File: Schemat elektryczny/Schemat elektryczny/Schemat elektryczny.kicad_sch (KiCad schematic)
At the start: 15 parts, among them M1 Pompa Membranowa R385: 1, M2 Pompa Membranowa R385: 2, M3 Motor_Servo MG-90S, Q2 BC107, Q3 BC107, U1 ESP32-WROOM-32, U10 HX711: 1, U2 Socket 230V AC, U3 Converter 230/12V AC/DC, U4 Converter 12/5V DC/DC, U5 Strain gauge: 3, U6 HX711: 3, U7 Strain gauge: 2, U8 HX711: 2, U9 Strain gauge: 1

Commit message: Squashed commit of the following:
commit 14932f831172e4170d33ec92addd128a30fe4f06
Author: Brajan Gąbka <104710627+Duke-Axer@users.noreply.github.com>
Date:   Sun Mar 23 11:26:04 2025 +0100

    Dodałem bibliotekę od serwomechanizmu i rozwinąłem funkcje od servo. Zmodyfikowałem schemat elektryczny. (#5)

    Co-authored-by: Brajan <b.gabka.nkn@gmail.com>
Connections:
- net at U6. (UCC): now also U1.25 (GPIO25); no longer U5. (A+)
- net at U10. (UCC): now also U1.27 (GPIO27); no longer U9. (A+)
- net at U2. (Neutral): now also U3. (-12V)
- net at U3. (-12V): now also M1.2 (-), M2.2 (-), U4. (-5V); no longer U2. (Neutral)
- net at U8. (UCC): now also U1.26 (GPIO26); no longer U7. (A+)
- new net: U5. (A+), U6. (UCC) (x3)
- new net: U10. (UCC), U9. (A+) (x3)
- new net: U2. (Neutral), U3. (-12V)
- new net: M3.2 (+), U1. (-5V), U4. (-5V)
- new net: M3.3 (-), U1. (-5V), U4. (-5V)
- new net: U10. (UCC), U6. (UCC), U8. (UCC)
- new net: U1. (-5V), U10. (UCC), U6. (UCC), U8. (UCC)
- new net: U1. (-5V), U1.22 (CLK), U10. (UCC), U6. (UCC), U8. (UCC)
- new net: U7. (A+), U8. (UCC) (x3)
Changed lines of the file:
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@@
 		(date "2025-03-21")
 		(company "Politechnika Lubelska")
-		(comment 1 "Patrycja Demianiuk")
-		(comment 2 "Daniel Cichocki")
-		(comment 3 "Brajan Gąbka")
+		(comment 1 "Inż Patrycja Demianiuk")
+		(comment 2 "Inż Daniel Cichocki")
+		(comment 3 "Inż Brajan Gąbka")
 		(comment 4 "Internet Rzeczy")
 		(comment 5 "Pani mgr inż. Aleksandra Wilczyńska")

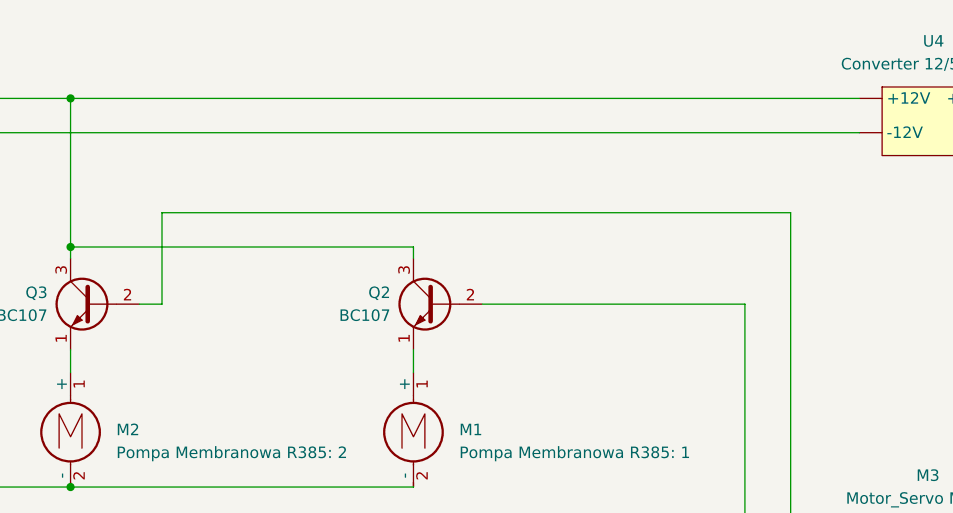
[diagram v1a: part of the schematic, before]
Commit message: Gabka (#11)
* dodałem plik .gitignore i usunąłem śledzenie folderu z schematów elektrycznych backups

* Dodałem rezystory do schematu

* Poprawiłem plik .gitignore

* Usuwam backups

---------

Co-authored-by: Brajan <b.gabka.nkn@gmail.com>
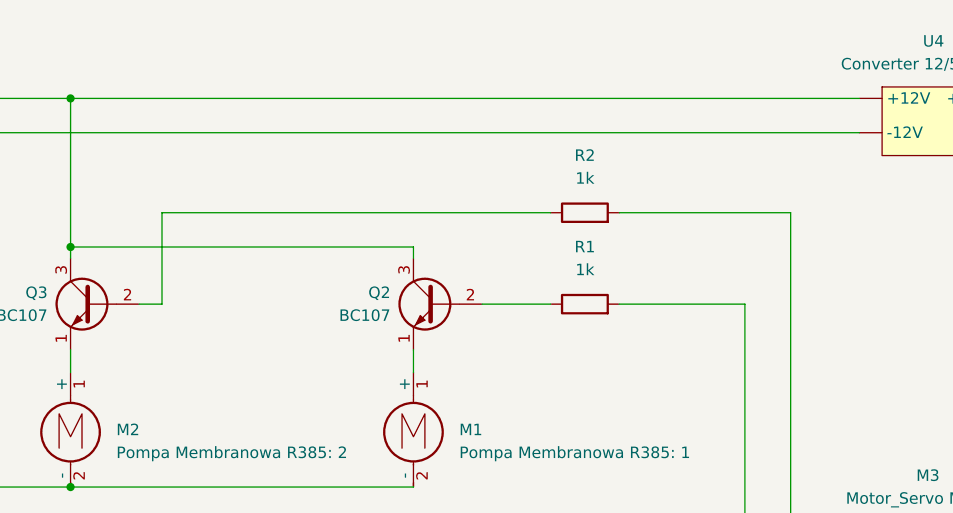
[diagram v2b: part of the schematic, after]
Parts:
- added R1, R2: 1k, symbol Device:R
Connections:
- net at U6. (UCC): now also U1.25 (GPIO25); no longer U5. (A+)
- net at Q3.2 (B): now also R2.1; no longer U1.14 (GPIO14)
- net at Q2.2 (B): now also R1.1; no longer U1.13 (GPIO13)
- net at U10. (UCC): now also U1.27 (GPIO27); no longer U9. (A+)
- net at U2. (Neutral): now also U3. (-12V)
- net at U3. (-12V): now also M1.2 (-), M2.2 (-), U4. (-5V); no longer U2. (Neutral)
- net at U8. (UCC): now also U1.26 (GPIO26); no longer U7. (A+)
- new net: U5. (A+), U6. (UCC) (x3)
- new net: U10. (UCC), U9. (A+) (x3)
- new net: U2. (Neutral), U3. (-12V)
- new net: M3.2 (+), U1. (-5V), U4. (-5V)
- new net: M3.3 (-), U1. (-5V), U4. (-5V)
- new net: U10. (UCC), U6. (UCC), U8. (UCC)
- new net: U1. (-5V), U10. (UCC), U6. (UCC), U8. (UCC)
- new net: U1. (-5V), U1.22 (CLK), U10. (UCC), U6. (UCC), U8. (UCC)
- new net: U7. (A+), U8. (UCC) (x3)
- new net: R1.2, U1.13 (GPIO13)
- new net: R2.2, U1.14 (GPIO14)
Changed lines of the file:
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@@
+	(wire
+		(pts
+			(xy 160.02 52.07) (xy 173.99 52.07)
+		)
+		(stroke
+			(width 0)
+			(type default)
+		)
+	)
 	(wire
 		(pts
@@
 	(wire
 		(pts
-			(xy 144.78 52.07) (xy 173.99 52.07)
-		)
-		(stroke
-			(width 0)
-			(type default)
-		)
-	)
-	(wire
-		(pts
-			(xy 179.07 41.91) (xy 109.22 41.91)
+			(xy 144.78 52.07) (xy 152.4 52.07)
+		)
+		(stroke
+			(width 0)
+			(type default)
+		)
+	)
+	(wire
+		(pts
+			(xy 179.07 41.91) (xy 160.02 41.91)
 		)
 		(stroke
@@
 		(pts
 			(xy 173.99 107.95) (xy 173.99 52.07)
+		)
+		(stroke
+			(width 0)
+			(type default)
+		)
+	)
+	(wire
+		(pts
+			(xy 152.4 41.91) (xy 109.22 41.91)
 		)
 		(stroke
@@
 					(unit 1)
 				)
+			)
+		)
+	)
+	(symbol
+		(lib_id "Device:R")
+		(at 156.21 52.07 90)
+		(unit 1)
+		(exclude_from_sim no)
+		(in_bom yes)
+		(on_board yes)
+		(dnp no)
+		(fields_autoplaced yes)
+		(property "Reference" "R1"
+			(at 156.21 45.72 90)
+			(effects
+				(font
+					(size 1.27 1.27)
+				)
+			)
+		)
+		(property "Value" "1k"
+			(at 156.21 48.26 90)
+			(effects
+				(font
+					(size 1.27 1.27)
+				)
+			)
+		)
+		(property "Footprint" ""
+			(at 156.21 53.848 90)
+			(effects
+				(font
+					(size 1.27 1.27)
+				)
+				(hide yes)
+			)
+		)
+		(property "Datasheet" "~"
+			(at 156.21 52.07 0)
+			(effects
+				(font
+					(size 1.27 1.27)
+				)
+				(hide yes)
+			)
+		)
+		(property "Description" "Resistor"
+			(at 156.21 52.07 0)
+			(effects
+				(font
+					(size 1.27 1.27)
+				)
+				(hide yes)
+			)
+		)
+		(pin "2"
+		)
+		(pin "1"
+		)
+		(instances
+			(project ""
+				(path "/052f1a03-7e75-4cf9-8b84-3452573b392a"
+					(reference "R1")
+					(unit 1)
+				)
+			)
+		)
+	)
+	(symbol
+		(lib_id "Device:R")
+		(at 156.21 41.91 90)
+		(unit 1)
+		(exclude_from_sim no)
+		(in_bom yes)
+		(on_board yes)
+		(dnp no)
+		(fields_autoplaced yes)
+		(property "Reference" "R2"
+			(at 156.21 35.56 90)
+			(effects
+				(font
+					(size 1.27 1.27)
+				)
+			)
+		)
+		(property "Value" "1k"
+			(at 156.21 38.1 90)
+			(effects
+				(font
+					(size 1.27 1.27)
+				)
+			)
+		)
+		(property "Footprint" ""
+			(at 156.21 43.688 90)
+			(effects
+				(font
+					(size 1.27 1.27)
+				)
+				(hide yes)
+			)
+		)
+		(property "Datasheet" "~"
+			(at 156.21 41.91 0)
+			(effects
+				(font
+					(size 1.27 1.27)
+				)
+				(hide yes)
+			)
+		)
+		(property "Description" "Resistor"
+			(at 156.21 41.91 0)
+			(effects
+				(font
+					(size 1.27 1.27)
+				)
+				(hide yes)
+			)
+		)
+		(pin "1"
+		)
+		(pin "2"
+		)
+		(instances
+			(project ""
+				(path "/052f1a03-7e75-4cf9-8b84-3452573b392a"
+					(reference "R2")
+					(unit 1)
+				)
